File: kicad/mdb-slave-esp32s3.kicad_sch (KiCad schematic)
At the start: 35 parts, among them J1 MDB_Connector, J2 USB_C_Receptacle_USB2.0_16P, J3 Conn_02x11_Odd_Even, SW1 SW_Push, U1 TLP785, U2 KA78M05_TO252, U3 ESP32-S3FH4R2, U4 TLP785, Y1 Crystal_GND24

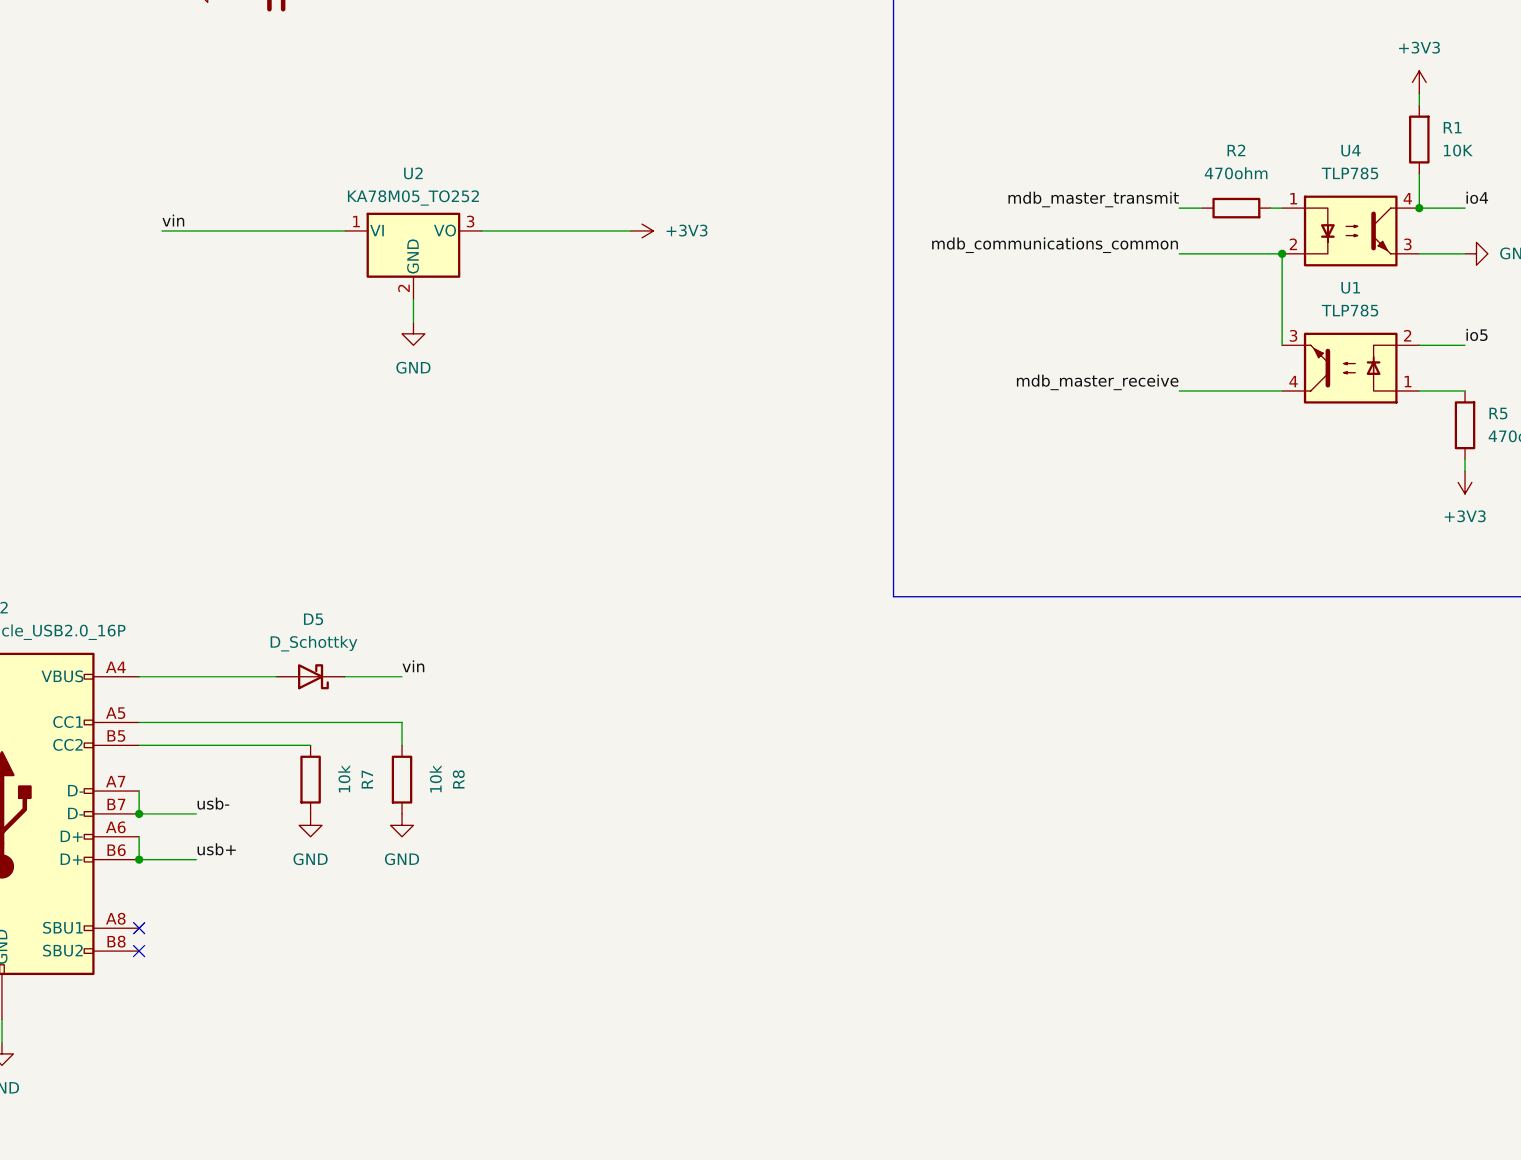
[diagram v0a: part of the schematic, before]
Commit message: Migrate from LDO regulator to conversor buck
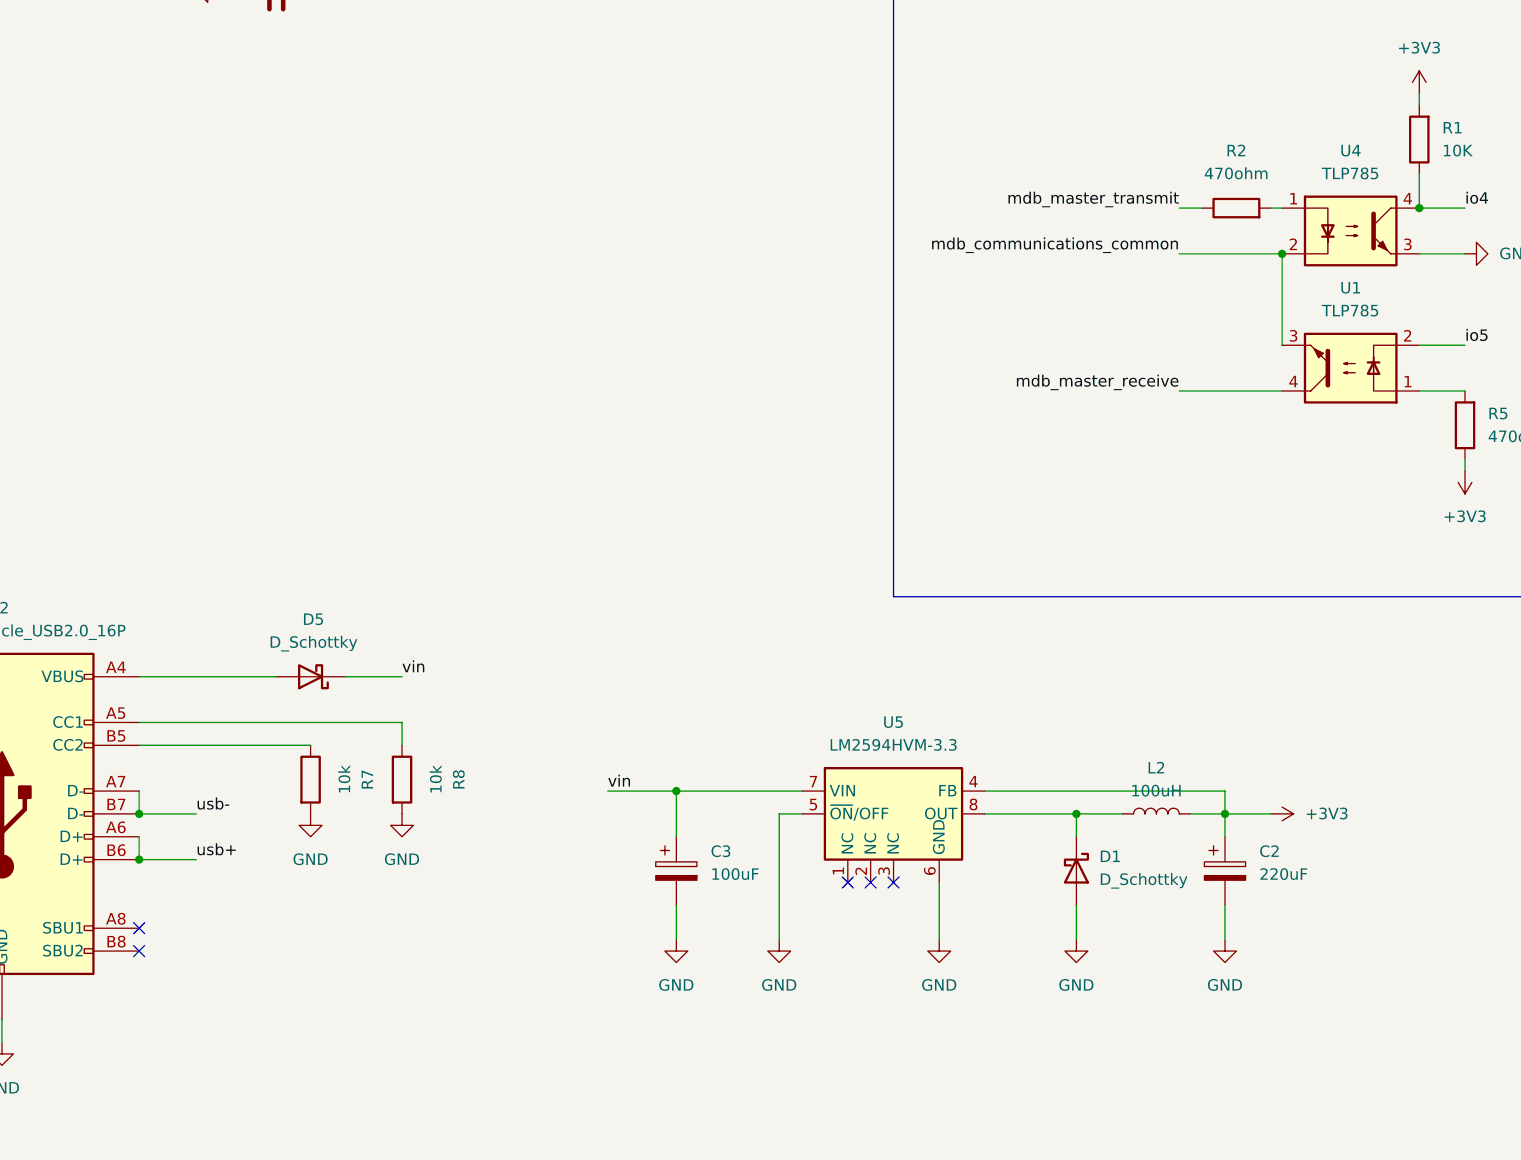
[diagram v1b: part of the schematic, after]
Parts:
- removed U2: KA78M05_TO252, Package_TO_SOT_SMD:TO-252-2, symbol Regulator_Linear:KA78M05_TO252
- added C2: 220uF, Capacitor_Tantalum_SMD:CP_EIA-3528-21_Kemet-B, symbol Device:C_Polarized
- added C3: 100uF, Capacitor_SMD:CP_Elec_6.3x5.8, symbol Device:C_Polarized
- added D1: D_Schottky, Diode_SMD:D_SOD-123, symbol Device:D_Schottky
- added L2: 100uH, Inductor_SMD:L_7.3x7.3_H3.5, symbol Device:L
- added U5: LM2594HVM-3.3, Package_SO:SOIC-8_3.9x4.9mm_P1.27mm, symbol Regulator_Switching:LM2594HVM-3.3
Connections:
- net +3V3: now also C2.1, L2.2, U5.4 (FB)
- net GND: now also C2.2, C3.2, D1.2 (A), U5.5 (~{ON}/OFF), U5.6 (GND)
- net vin: now also C3.1, U5.7 (VIN)
- new net: D1.1 (K), L2.1, U5.8 (OUT)
- no-connect marks 26 -> 29

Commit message: Updating bill of materials
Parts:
- C2: #LCSC C30242 -> (none); LCSC# (none) -> C30242
- C3: #LCSC C128464 -> (none); LCSC# (none) -> C128464
- L2: #LCSC C182195 -> (none); LCSC# (none) -> C182195
- U5: #LCSC C18057294 -> (none); LCSC# (none) -> C18057294

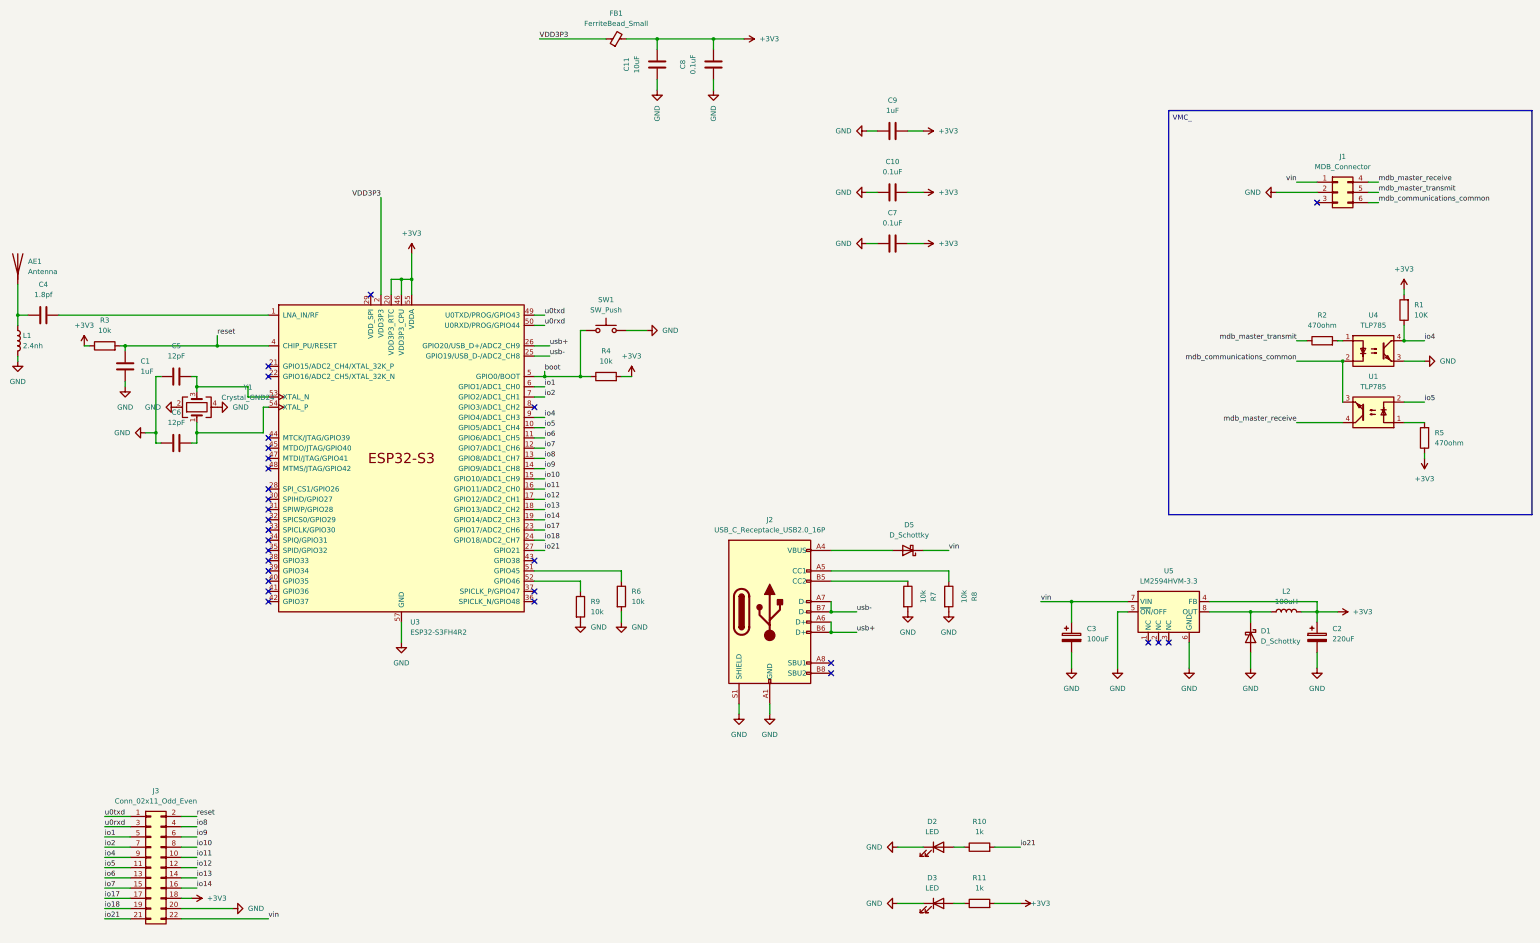
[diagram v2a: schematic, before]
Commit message: Adding buzzer and ws2812b LED Addressable
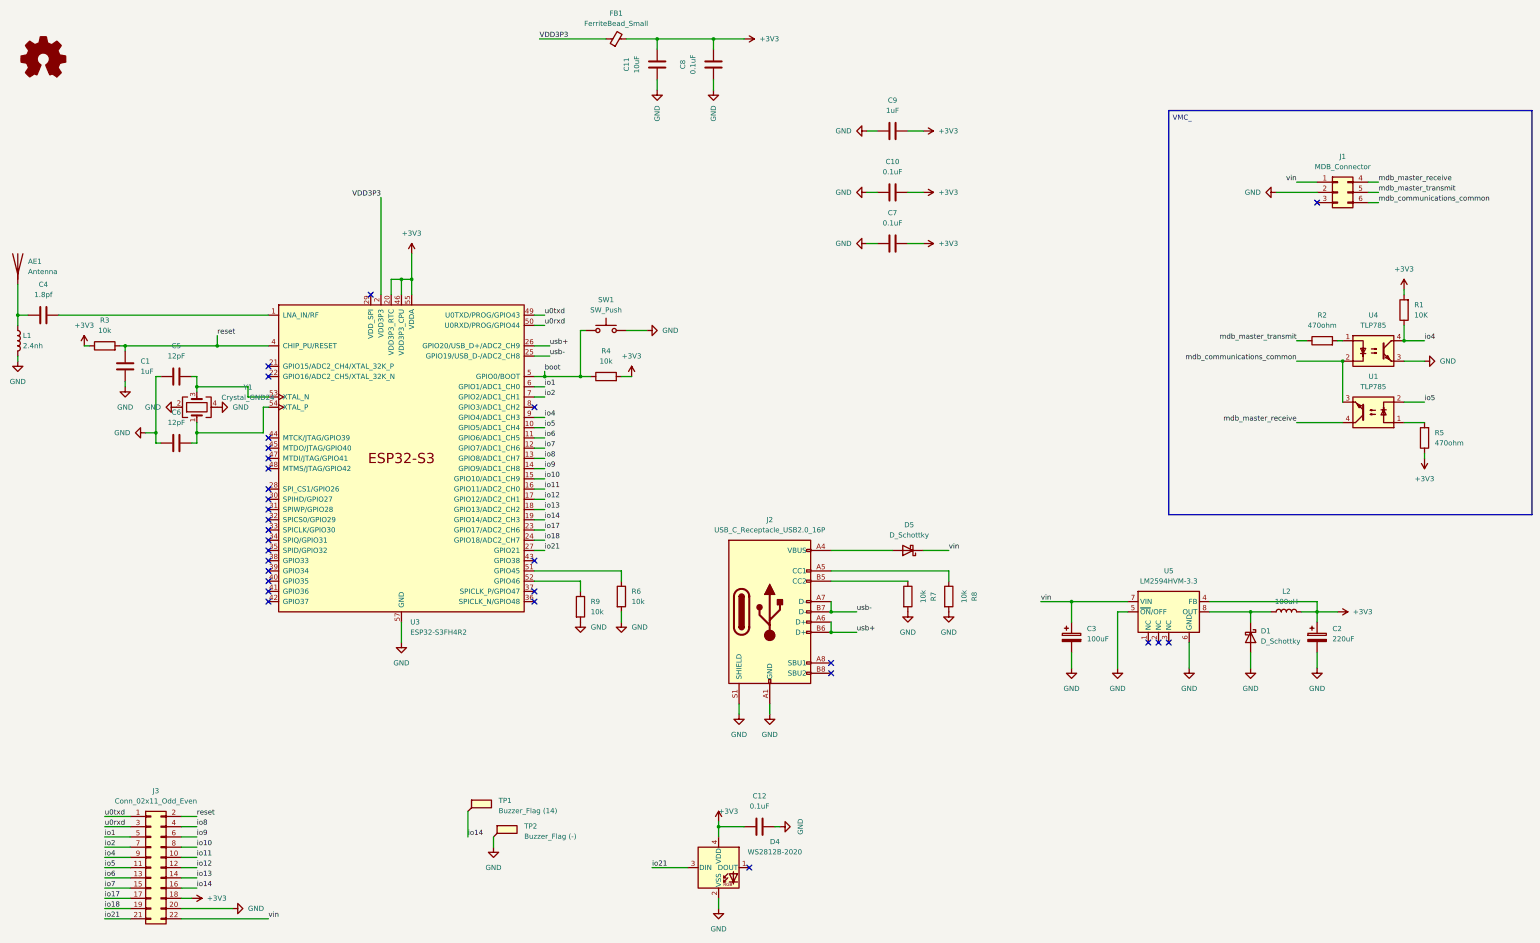
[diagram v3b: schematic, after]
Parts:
- removed D2, D3: LED, LED_SMD:LED_0603_1608Metric, symbol Device:LED
- removed R10, R11: 1k, Resistor_SMD:R_0603_1608Metric, symbol Device:R
- added C12: 0.1uF, Capacitor_SMD:C_0603_1608Metric, symbol Device:C
- added D4: WS2812B-2020, LED_SMD:LED_WS2812B-2020_PLCC4_2.0x2.0mm, symbol LED:WS2812B-2020
- added TP1: Buzzer_Flag (14), TestPoint:TestPoint_Pad_3.0x3.0mm, symbol Connector:TestPoint_Flag
- added TP2: Buzzer_Flag (-), TestPoint:TestPoint_Pad_3.0x3.0mm, symbol Connector:TestPoint_Flag
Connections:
- net +3V3: now also C12.2, D4.4 (VDD)
- net GND: now also C12.1, D4.2 (VSS), TP2.1
- net io14: now also TP1.1
- net io21: now also D4.3 (DIN)
- no-connect marks 29 -> 30

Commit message: XINGLIGHT XL-2121RGBC-2812B LED Addressable
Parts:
- D4: LCSC# C965555 -> C5349957
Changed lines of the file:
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@@
 			)
 		)
-		(property "LCSC#" "C965555"
+		(property "LCSC#" "C5349957"
 			(at 203.2 236.22 0)
 			(effects

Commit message: Aligning components
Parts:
- TP1, TP2: footprint TestPoint:TestPoint_Pad_3.0x3.0mm -> TestPoint:TestPoint_Pad_2.0x2.0mm
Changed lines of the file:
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@@
 			)
 		)
-		(property "Footprint" "TestPoint:TestPoint_Pad_3.0x3.0mm"
+		(property "Footprint" "TestPoint:TestPoint_Pad_2.0x2.0mm"
 			(at 146.05 222.25 0)
 			(effects
@@
 			)
 		)
-		(property "Footprint" "TestPoint:TestPoint_Pad_3.0x3.0mm"
+		(property "Footprint" "TestPoint:TestPoint_Pad_2.0x2.0mm"
 			(at 152.4 228.6 0)
 			(effects

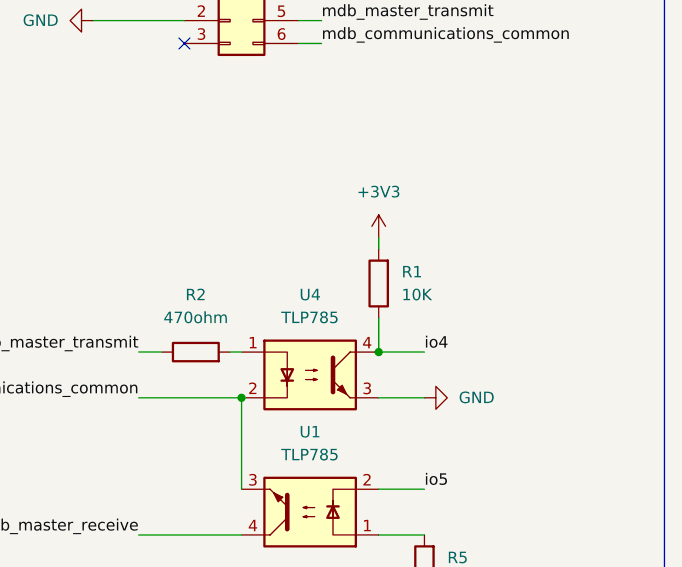
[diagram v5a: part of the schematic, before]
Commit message: bug fixing - Changing 10k resistor -> 1k resistor
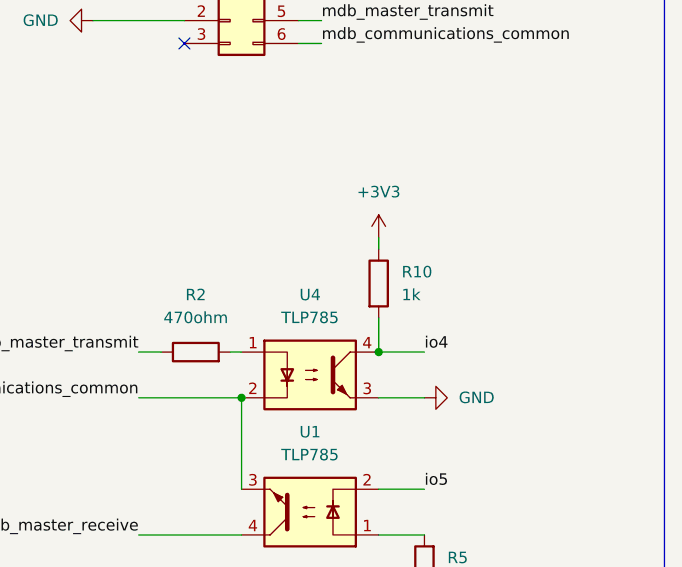
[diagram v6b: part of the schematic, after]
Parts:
- removed R1: 10K, Resistor_SMD:R_0603_1608Metric, symbol Device:R
- added R10: 1k, Resistor_SMD:R_0603_1608Metric, symbol Device:R
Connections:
- net +3V3: now also R10.1
- net io4: now also R10.2

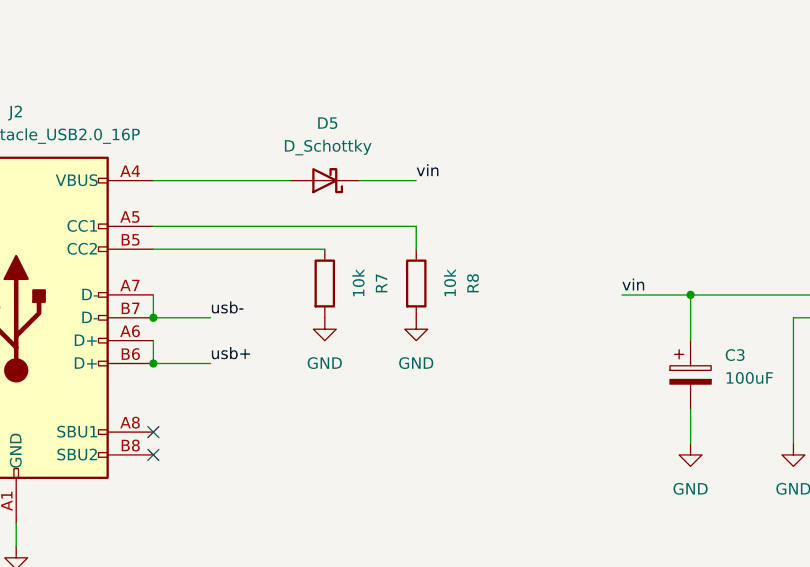
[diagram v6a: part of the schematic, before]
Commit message: Fixing usb-c <-> usb-c communication error: Resistor 10k -> 5.1k
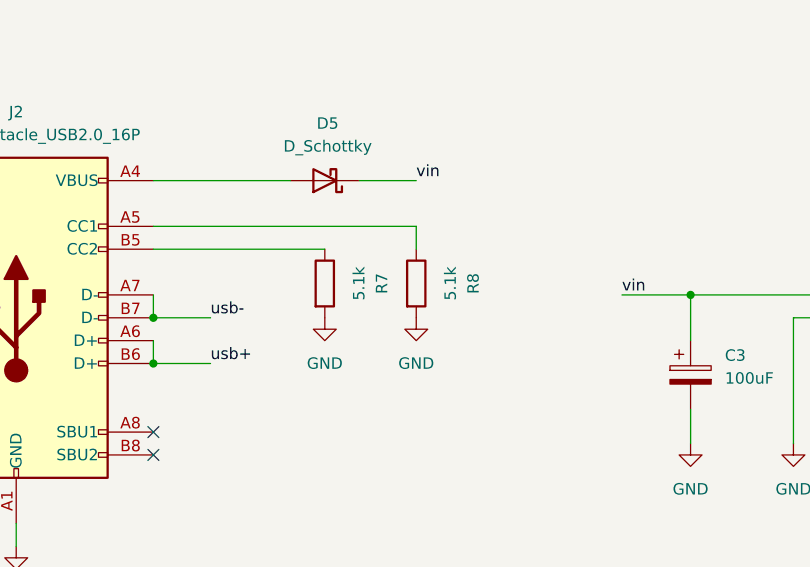
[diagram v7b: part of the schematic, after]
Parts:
- R7: value 10k -> 5.1k
- R8: value 10k -> 5.1k; LCSC# C98220 -> C394543
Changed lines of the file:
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@@
 			)
 		)
-		(property "Value" "10k"
+		(property "Value" "5.1k"
 			(at 264.16 168.91 90)
 			(effects
@@
 			)
 		)
-		(property "LCSC#" "C98220"
+		(property "LCSC#" "C394543"
 			(at 260.35 168.91 90)
 			(effects
@@
 			)
 		)
-		(property "Value" "10k"
+		(property "Value" "5.1k"
 			(at 254 168.91 90)
 			(effects

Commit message: Fixing usb-c <-> usb-c communication error: Resistor 10k -> 5.1k
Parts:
- R7: LCSC# C98220 -> C394543
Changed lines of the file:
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@@
 			)
 		)
-		(property "LCSC#" "C98220"
+		(property "LCSC#" "C394543"
 			(at 250.19 168.91 90)
 			(effects
